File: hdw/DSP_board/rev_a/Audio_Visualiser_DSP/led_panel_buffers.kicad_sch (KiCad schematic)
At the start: 29 parts

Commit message: Annotated schematic
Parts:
- gave numbers to parts that had none: 29

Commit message: cleared stale digikey part numbers
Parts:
- C1801, C1802, C1803, C1804, C1805, C1806: Digi-Key PN 490-10697-1-ND -> (none)
- C1807, C1808, C1809, C1810, C1811: footprint Capacitors_SMD:C_0603 -> Capacitors_SMD:C_0402; Digi-Key PN 1276-1935-1-ND -> (none)
- R1801, R1802, R1803, R1804, R1805: Digi-Key PN 541-100KHCT-ND -> (none)
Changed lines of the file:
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@@
 			)
 		)
-		(property "Digi-Key PN" "490-10697-1-ND"
+		(property "Digi-Key PN" ""
 			(at 51.435 171.45 0)
 			(hide yes)
@@
 			)
 		)
-		(property "Digi-Key PN" "490-10697-1-ND"
+		(property "Digi-Key PN" ""
 			(at 66.675 54.61 0)
 			(hide yes)
@@
 			)
 		)
-		(property "Footprint" "Capacitors_SMD:C_0603"
+		(property "Footprint" "Capacitors_SMD:C_0402"
 			(at 238.4552 80.01 0)
 			(hide yes)
@@
 			)
 		)
-		(property "Digi-Key PN" "1276-1935-1-ND"
+		(property "Digi-Key PN" ""
 			(at 248.285 63.5 0)
 			(hide yes)
@@
 			)
 		)
-		(property "Digi-Key PN" "490-10697-1-ND"
+		(property "Digi-Key PN" ""
 			(at 51.435 146.05 0)
 			(hide yes)
@@
 			)
 		)
-		(property "Footprint" "Capacitors_SMD:C_0603"
+		(property "Footprint" "Capacitors_SMD:C_0402"
 			(at 221.9452 156.21 0)
 			(hide yes)
@@
 			)
 		)
-		(property "Digi-Key PN" "1276-1935-1-ND"
+		(property "Digi-Key PN" ""
 			(at 231.775 139.7 0)
 			(hide yes)
@@
 			)
 		)
-		(property "Digi-Key PN" "541-100KHCT-ND"
+		(property "Digi-Key PN" ""
 			(at 44.45 179.07 0)
 			(hide yes)
@@
 			)
 		)
-		(property "Footprint" "Capacitors_SMD:C_0603"
+		(property "Footprint" "Capacitors_SMD:C_0402"
 			(at 205.4352 156.21 0)
 			(hide yes)
@@
 			)
 		)
-		(property "Digi-Key PN" "1276-1935-1-ND"
+		(property "Digi-Key PN" ""
 			(at 215.265 139.7 0)
 			(hide yes)
@@
 			)
 		)
-		(property "Digi-Key PN" "541-100KHCT-ND"
+		(property "Digi-Key PN" ""
 			(at 114.3 153.67 0)
 			(hide yes)
@@
 			)
 		)
-		(property "Footprint" "Capacitors_SMD:C_0603"
+		(property "Footprint" "Capacitors_SMD:C_0402"
 			(at 205.4352 67.31 0)
 			(hide yes)
@@
 			)
 		)
-		(property "Digi-Key PN" "1276-1935-1-ND"
+		(property "Digi-Key PN" ""
 			(at 215.265 50.8 0)
 			(hide yes)
@@
 			)
 		)
-		(property "Footprint" "Capacitors_SMD:C_0603"
+		(property "Footprint" "Capacitors_SMD:C_0402"
 			(at 221.9452 67.31 0)
 			(hide yes)
@@
 			)
 		)
-		(property "Digi-Key PN" "1276-1935-1-ND"
+		(property "Digi-Key PN" ""
 			(at 231.775 50.8 0)
 			(hide yes)
@@
 			)
 		)
-		(property "Digi-Key PN" "490-10697-1-ND"
+		(property "Digi-Key PN" ""
 			(at 121.285 171.45 0)
 			(hide yes)
@@
 			)
 		)
-		(property "Digi-Key PN" "541-100KHCT-ND"
+		(property "Digi-Key PN" ""
 			(at 114.3 179.07 0)
 			(hide yes)
@@
 			)
 		)
-		(property "Digi-Key PN" "541-100KHCT-ND"
+		(property "Digi-Key PN" ""
 			(at 44.45 153.67 0)
 			(hide yes)
@@
 			)
 		)
-		(property "Digi-Key PN" "490-10697-1-ND"
+		(property "Digi-Key PN" ""
 			(at 66.675 110.49 0)
 			(hide yes)
@@
 			)
 		)
-		(property "Digi-Key PN" "490-10697-1-ND"
+		(property "Digi-Key PN" ""
 			(at 121.285 146.05 0)
 			(hide yes)
@@
 			)
 		)
-		(property "Digi-Key PN" "541-100KHCT-ND"
+		(property "Digi-Key PN" ""
 			(at 220.98 96.52 0)
 			(hide yes)

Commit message: assigned some footprints
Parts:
- U1803, U1804: footprint (none) -> Package_DFN_QFN:DHVQFN-20-1EP_2.5x4.5mm_P0.5mm_EP1x3mm

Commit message: assigned many digi-key part numbers
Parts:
- C1801, C1802, C1803, C1804, C1805, C1806, C1807, C1808, C1809, C1810, C1811: Digi-Key PN (none) -> 1276-CL05B104KB5NNNCCT-ND
- R1801, R1802, R1803, R1804, R1805: Digi-Key PN (none) -> 311-10.0KLRCT-ND
- RN1801, RN1802, RN1803, RN1804: Digi-Key PN (none) -> Y1103CT-ND
- U1801, U1802, U1805, U1806, U1808: Digi-Key PN (none) -> 296-15582-1-ND
- U1807, U1809: Digi-Key PN (none) -> 296-47829-1-ND
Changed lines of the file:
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@@
 			)
 		)
-		(property "Digi-Key PN" ""
+		(property "Digi-Key PN" "1276-CL05B104KB5NNNCCT-ND"
 			(at 51.435 171.45 0)
 			(hide yes)
@@
 			)
 		)
-		(property "Digi-Key PN" ""
+		(property "Digi-Key PN" "1276-CL05B104KB5NNNCCT-ND"
 			(at 66.675 54.61 0)
 			(hide yes)
@@
 			)
 		)
-		(property "Digi-Key PN" ""
+		(property "Digi-Key PN" "1276-CL05B104KB5NNNCCT-ND"
 			(at 248.285 63.5 0)
 			(hide yes)
@@
 			)
 		)
-		(property "Digi-Key PN" ""
+		(property "Digi-Key PN" "1276-CL05B104KB5NNNCCT-ND"
 			(at 51.435 146.05 0)
 			(hide yes)
@@
 			)
 		)
+		(property "Digi-Key PN" "296-15582-1-ND"
+			(at 53.34 172.72 0)
+			(hide yes)
+			(show_name no)
+			(do_not_autoplace no)
+			(effects
+				(font
+					(size 1.27 1.27)
+				)
+			)
+		)
 		(pin "2"
 		)
@@
 			)
 		)
+		(property "Digi-Key PN" "Y1103CT-ND"
+			(at 58.42 59.69 0)
+			(hide yes)
+			(show_name no)
+			(do_not_autoplace no)
+			(effects
+				(font
+					(size 1.27 1.27)
+				)
+			)
+		)
 		(pin "14"
 		)
@@
 			)
 		)
-		(property "Digi-Key PN" ""
+		(property "Digi-Key PN" "1276-CL05B104KB5NNNCCT-ND"
 			(at 231.775 139.7 0)
 			(hide yes)
@@
 			)
 		)
+		(property "Digi-Key PN" "296-15582-1-ND"
+			(at 212.09 90.17 0)
+			(hide yes)
+			(show_name no)
+			(do_not_autoplace no)
+			(effects
+				(font
+					(size 1.27 1.27)
+				)
+			)
+		)
 		(pin "3"
 		)
@@
 			)
 		)
+		(property "Digi-Key PN" "296-15582-1-ND"
+			(at 123.19 172.72 0)
+			(hide yes)
+			(show_name no)
+			(do_not_autoplace no)
+			(effects
+				(font
+					(size 1.27 1.27)
+				)
+			)
+		)
 		(pin "2"
 		)
@@
 			)
 		)
-		(property "Digi-Key PN" ""
+		(property "Digi-Key PN" "311-10.0KLRCT-ND"
 			(at 44.45 179.07 0)
 			(hide yes)
@@
 			)
 		)
-		(property "Digi-Key PN" ""
+		(property "Digi-Key PN" "1276-CL05B104KB5NNNCCT-ND"
 			(at 215.265 139.7 0)
 			(hide yes)
@@
 			)
 		)
-		(property "Digi-Key PN" ""
+		(property "Digi-Key PN" "311-10.0KLRCT-ND"
 			(at 114.3 153.67 0)
 			(hide yes)
@@
 			)
 		)
+		(property "Digi-Key PN" "296-47829-1-ND"
+			(at 212.09 36.83 0)
+			(hide yes)
+			(show_name no)
+			(do_not_autoplace no)
+			(effects
+				(font
+					(size 1.27 1.27)
+				)
+			)
+		)
 		(pin "1"
 		)
@@
 			)
 		)
-		(property "Digi-Key PN" ""
+		(property "Digi-Key PN" "1276-CL05B104KB5NNNCCT-ND"
 			(at 215.265 50.8 0)
 			(hide yes)
@@
 			)
 		)
+		(property "Digi-Key PN" "296-47829-1-ND"
+			(at 212.09 125.73 0)
+			(hide yes)
+			(show_name no)
+			(do_not_autoplace no)
+			(effects
+				(font
+					(size 1.27 1.27)
+				)
+			)
+		)
 		(pin "1"
 		)
@@
 			)
 		)
-		(property "Digi-Key PN" ""
+		(property "Digi-Key PN" "1276-CL05B104KB5NNNCCT-ND"
 			(at 231.775 50.8 0)
 			(hide yes)
@@
 			)
 		)
+		(property "Digi-Key PN" "Y1103CT-ND"
+			(at 116.84 59.69 0)
+			(hide yes)
+			(show_name no)
+			(do_not_autoplace no)
+			(effects
+				(font
+					(size 1.27 1.27)
+				)
+			)
+		)
 		(pin "14"
 		)
@@
 			)
 		)
-		(property "Digi-Key PN" ""
+		(property "Digi-Key PN" "1276-CL05B104KB5NNNCCT-ND"
 			(at 121.285 171.45 0)
 			(hide yes)
@@
 			)
 		)
-		(property "Digi-Key PN" ""
+		(property "Digi-Key PN" "311-10.0KLRCT-ND"
 			(at 114.3 179.07 0)
 			(hide yes)
@@
 			)
 		)
-		(property "Digi-Key PN" ""
+		(property "Digi-Key PN" "311-10.0KLRCT-ND"
 			(at 44.45 153.67 0)
 			(hide yes)
@@
 			)
 		)
+		(property "Digi-Key PN" "Y1103CT-ND"
+			(at 116.84 115.57 0)
+			(hide yes)
+			(show_name no)
+			(do_not_autoplace no)
+			(effects
+				(font
+					(size 1.27 1.27)
+				)
+			)
+		)
 		(pin "14"
 		)
@@
 			)
 		)
-		(property "Digi-Key PN" ""
+		(property "Digi-Key PN" "1276-CL05B104KB5NNNCCT-ND"
 			(at 66.675 110.49 0)
 			(hide yes)
@@
 			)
 		)
+		(property "Digi-Key PN" "296-15582-1-ND"
+			(at 53.34 147.32 0)
+			(hide yes)
+			(show_name no)
+			(do_not_autoplace no)
+			(effects
+				(font
+					(size 1.27 1.27)
+				)
+			)
+		)
 		(pin "2"
 		)
@@
 			)
 		)
+		(property "Digi-Key PN" "Y1103CT-ND"
+			(at 58.42 115.57 0)
+			(hide yes)
+			(show_name no)
+			(do_not_autoplace no)
+			(effects
+				(font
+					(size 1.27 1.27)
+				)
+			)
+		)
 		(pin "14"
 		)
@@
 			)
 		)
+		(property "Digi-Key PN" "296-15582-1-ND"
+			(at 123.19 147.32 0)
+			(hide yes)
+			(show_name no)
+			(do_not_autoplace no)
+			(effects
+				(font
+					(size 1.27 1.27)
+				)
+			)
+		)
 		(pin "2"
 		)
@@
 			)
 		)
-		(property "Digi-Key PN" ""
+		(property "Digi-Key PN" "1276-CL05B104KB5NNNCCT-ND"
 			(at 121.285 146.05 0)
 			(hide yes)
@@
 			)
 		)
-		(property "Digi-Key PN" ""
+		(property "Digi-Key PN" "311-10.0KLRCT-ND"
 			(at 220.98 96.52 0)
 			(hide yes)

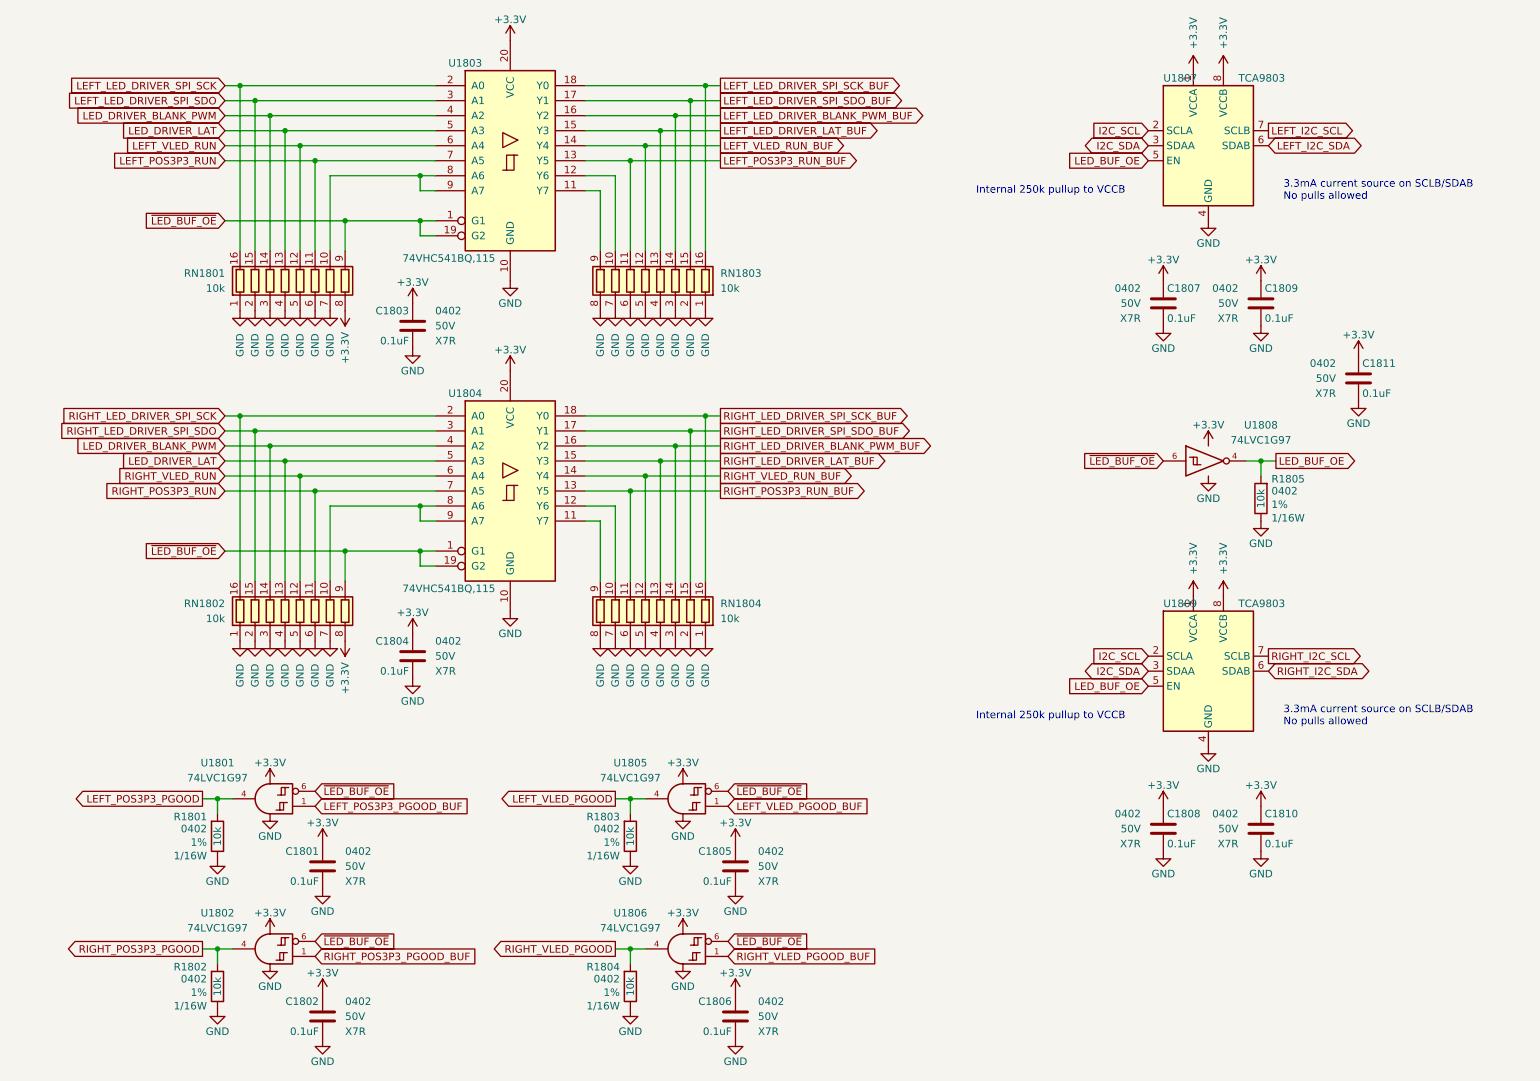
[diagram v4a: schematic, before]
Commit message: Added a bunch of stuff to the schematic
Moved to adafruit I2C rotary encoder module. Added signal test points. Added some design schematic notes. Added LEd output connector ESD diodes. Consolidated on a single schottky diode. Connected most signals to MCU
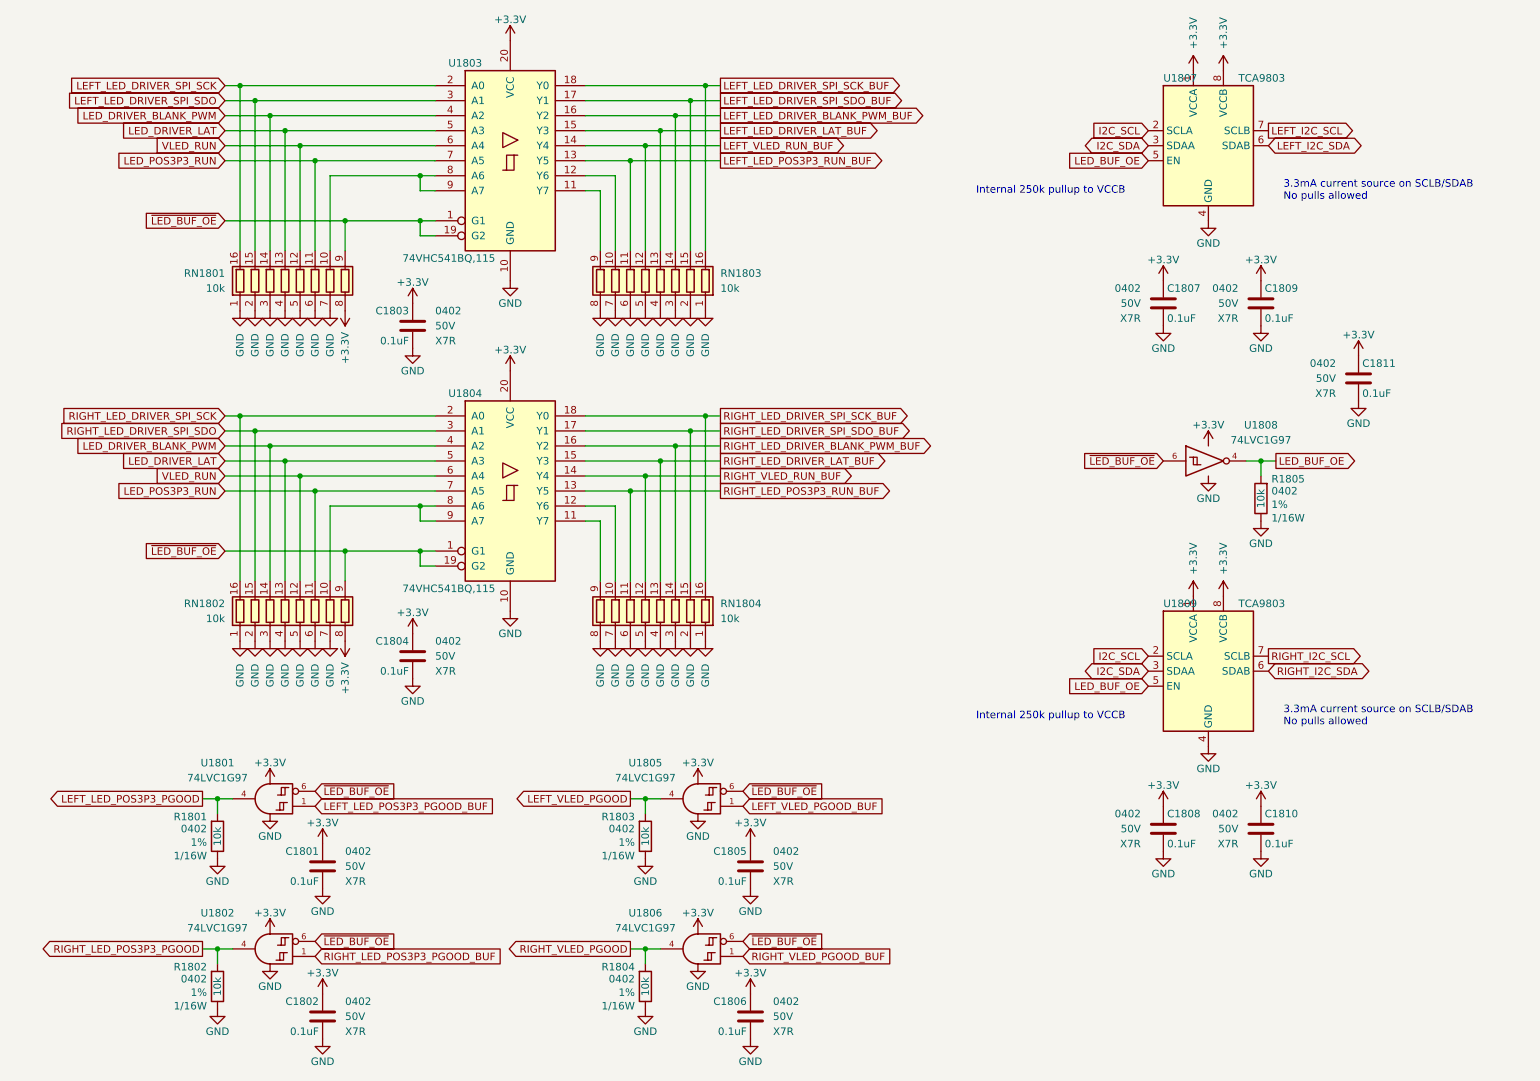
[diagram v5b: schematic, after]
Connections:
- net RIGHT_POS3P3_RUN is gone; now on net LED_POS3P3_RUN: RN1802.11 (R6.2), U1804.7 (A5)
- net RIGHT_VLED_RUN is gone; now on net VLED_RUN: RN1802.12 (R5.2), U1804.6 (A4)
- net LEFT_POS3P3_PGOOD renamed LEFT_LED_POS3P3_PGOOD
- net LEFT_POS3P3_PGOOD_BUF renamed LEFT_LED_POS3P3_PGOOD_BUF
- net LEFT_POS3P3_RUN renamed LED_POS3P3_RUN
- net LEFT_POS3P3_RUN_BUF renamed LEFT_LED_POS3P3_RUN_BUF
- net LEFT_VLED_RUN renamed VLED_RUN
- net RIGHT_POS3P3_PGOOD renamed RIGHT_LED_POS3P3_PGOOD
- net RIGHT_POS3P3_PGOOD_BUF renamed RIGHT_LED_POS3P3_PGOOD_BUF
- net RIGHT_POS3P3_RUN_BUF renamed RIGHT_LED_POS3P3_RUN_BUF
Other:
- moved on the sheet: C1805, C1806, R1803, R1804, U1805, U1806

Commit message: fix a lot of digikey pns which are out of stock, find alternate inductors, change I2C buffers
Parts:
- U1807, U1809: value TCA9803 -> TCA9801; Digi-Key PN 296-47829-1-ND -> 296-47828-1-ND
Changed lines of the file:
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@@
 			)
 		)
-		(property "Value" "TCA9803"
+		(property "Value" "TCA9801"
 			(at 217.17 25.4 0)
 			(show_name no)
@@
 			)
 		)
-		(property "Digi-Key PN" "296-47829-1-ND"
+		(property "Digi-Key PN" "296-47828-1-ND"
 			(at 212.09 36.83 0)
 			(hide yes)
@@
 			)
 		)
-		(property "Value" "TCA9803"
+		(property "Value" "TCA9801"
 			(at 217.17 114.3 0)
 			(show_name no)
@@
 			)
 		)
-		(property "Digi-Key PN" "296-47829-1-ND"
+		(property "Digi-Key PN" "296-47828-1-ND"
 			(at 212.09 125.73 0)
 			(hide yes)
